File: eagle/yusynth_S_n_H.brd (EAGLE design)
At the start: 100 x 80 mm, 43 parts, among them IC1 TL074P, IC2 TL071P, Q1 BF245, T1 2N3904

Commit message: routed
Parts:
- moved R11 10.7 mm to (66.8, 34.3)
- moved C7 3.94 mm to (69.8, 33.3)
- moved LED1 2.05 mm to (44.2, 53.8)
- moved U$1 1.78 mm to (25.4, 55.4)
- moved R5 1.61 mm to (62.0, 46.2)
- moved R8 1.37 mm to (65.4, 40.1)
- moved R7 1.14 mm to (68.3, 42.7)
- moved C9 0.76 mm to (55.1, 41.9)
- moved R2 0.76 mm to (54.6, 53.8)
- moved R3 0.51 mm to (66.5, 25.4)
- turned C1 to 180 degrees
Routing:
- net -12V: track 62.9 -> 106.1 mm, vias 0 -> 2
- net GND: track 379.4 -> 369.5 mm
- net N$3: track 55.1 -> 46.4 mm
- net N$10: track 36.5 -> 29.1 mm
- net N$21: track 34.4 -> 27.2 mm, vias 2 -> 0
- net N$7: track 13.9 -> 11.8 mm
- net N$13: track 58.5 -> 56.5 mm
- net N$8: track 6.07 -> 4.17 mm
- net N$1: track 13.3 -> 11.9 mm
- net N$4: track 62.1 -> 63.3 mm
- net N$5: track 6.02 -> 5.08 mm
- net N$19: track 68.9 -> 68.2 mm
- net N$15: track 11.8 -> 11.2 mm

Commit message: cutout
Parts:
- moved SLEW 1.27 mm to (82.5, 3.81)
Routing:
- net GND: track 369.5 -> 373.4 mm
- net N$19: track 68.2 -> 69.5 mm
- net N$13: track 56.5 -> 57.7 mm
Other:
- board size 100 x 80 mm -> 100 x 81 mm
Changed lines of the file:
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@@
 <layer number="44" name="Drills" color="7" fill="1" visible="no" active="yes"/>
 <layer number="45" name="Holes" color="7" fill="1" visible="no" active="yes"/>
-<layer number="46" name="Milling" color="3" fill="1" visible="no" active="yes"/>
+<layer number="46" name="Milling" color="3" fill="1" visible="yes" active="yes"/>
 <layer number="47" name="Measures" color="7" fill="1" visible="no" active="yes"/>
 <layer number="48" name="Document" color="7" fill="1" visible="yes" active="yes"/>
@@
 <wire x1="100" y1="80" x2="0" y2="80" width="0" layer="20"/>
 <wire x1="0" y1="80" x2="0" y2="0" width="0" layer="20"/>
+<wire x1="2.286" y1="-1.016" x2="1.016" y2="0.762" width="1.6764" layer="46"/>
+<wire x1="1.016" y1="0.762" x2="1.016" y2="60.96" width="1.6764" layer="46"/>
+<wire x1="1.016" y1="60.96" x2="2.54" y2="62.23" width="1.6764" layer="46"/>
+<wire x1="2.54" y1="62.23" x2="90.424" y2="62.23" width="1.6764" layer="46"/>
+<wire x1="90.424" y1="62.23" x2="91.694" y2="60.452" width="1.6764" layer="46"/>
+<wire x1="91.694" y1="60.452" x2="91.694" y2="1.524" width="1.6764" layer="46"/>
+<wire x1="91.694" y1="1.524" x2="89.408" y2="-1.016" width="1.6764" layer="46"/>
+<wire x1="89.408" y1="-1.016" x2="2.286" y2="-1.016" width="1.6764" layer="46"/>
+<wire x1="5.08" y1="58.42" x2="4.572" y2="58.42" width="1.6764" layer="46"/>
+<wire x1="4.572" y1="58.42" x2="4.318" y2="58.166" width="1.6764" layer="46"/>
+<wire x1="4.318" y1="58.166" x2="4.318" y2="57.404" width="1.6764" layer="46"/>
+<wire x1="4.318" y1="57.404" x2="4.572" y2="57.15" width="1.6764" layer="46"/>
+<wire x1="4.572" y1="57.15" x2="5.08" y2="57.15" width="1.6764" layer="46"/>
+<wire x1="5.08" y1="57.15" x2="5.588" y2="57.658" width="1.6764" layer="46"/>
+<wire x1="5.588" y1="57.658" x2="5.588" y2="58.42" width="1.6764" layer="46"/>
+<wire x1="87.376" y1="58.928" x2="86.868" y2="58.928" width="1.6764" layer="46"/>
+<wire x1="86.868" y1="58.928" x2="86.614" y2="58.674" width="1.6764" layer="46"/>
+<wire x1="86.614" y1="58.674" x2="86.614" y2="57.912" width="1.6764" layer="46"/>
+<wire x1="86.614" y1="57.912" x2="86.868" y2="57.658" width="1.6764" layer="46"/>
+<wire x1="86.868" y1="57.658" x2="87.376" y2="57.658" width="1.6764" layer="46"/>
+<wire x1="87.376" y1="57.658" x2="87.884" y2="58.166" width="1.6764" layer="46"/>
+<wire x1="87.884" y1="58.166" x2="87.884" y2="58.928" width="1.6764" layer="46"/>
+<wire x1="5.334" y1="4.064" x2="4.826" y2="4.064" width="1.6764" layer="46"/>
+<wire x1="4.826" y1="4.064" x2="4.572" y2="3.81" width="1.6764" layer="46"/>
+<wire x1="4.572" y1="3.81" x2="4.572" y2="3.048" width="1.6764" layer="46"/>
+<wire x1="4.572" y1="3.048" x2="4.826" y2="2.794" width="1.6764" layer="46"/>
+<wire x1="4.826" y1="2.794" x2="5.334" y2="2.794" width="1.6764" layer="46"/>
+<wire x1="5.334" y1="2.794" x2="5.842" y2="3.302" width="1.6764" layer="46"/>
+<wire x1="5.842" y1="3.302" x2="5.842" y2="4.064" width="1.6764" layer="46"/>
 </plain>
 <attributes>
@@
 <element name="R8" library="rcl" package="0207/10" value="100k" x="65.405" y="40.132"/>
 <element name="R9" library="rcl" package="0207/10" value="100k" x="51.435" y="20.955" rot="R90"/>
-<element name="SLEW" library="pot" package="3RP/1610N" value="1M log" x="82.55" y="5.08"/>
+<element name="SLEW" library="pot" package="3RP/1610N" value="1M log" x="82.55" y="3.81"/>
 <element name="T1" library="transistor" package="TO92" value="2N3904" x="55.88" y="49.53" rot="R270"/>
 <element name="U$1" library="adafruit" package="FB" value="FB" x="25.4" y="55.372"/>
@@
 <wire x1="72.5424" y1="40.64" x2="72.5424" y2="42.672" width="0.8128" layer="16"/>
 <wire x1="89.6112" y1="23.1648" x2="72.5424" y2="40.2336" width="0.8128" layer="16"/>
-<wire x1="89.6112" y1="4.2672" x2="89.6112" y2="23.1648" width="0.8128" layer="16"/>
-<wire x1="88.392" y1="3.048" x2="89.6112" y2="4.2672" width="0.8128" layer="16"/>
-<wire x1="81.6864" y1="3.048" x2="88.392" y2="3.048" width="0.8128" layer="16"/>
-<wire x1="79.8576" y1="4.8768" x2="81.6864" y2="3.048" width="0.8128" layer="16"/>
-<wire x1="79.8576" y1="6.096" x2="79.8576" y2="4.8768" width="0.8128" layer="16"/>
+<wire x1="89.6112" y1="2.7432" x2="89.6112" y2="23.1648" width="0.8128" layer="16"/>
+<wire x1="88.392" y1="1.016" x2="89.6112" y2="2.7432" width="0.8128" layer="16"/>
+<wire x1="81.6864" y1="1.016" x2="88.392" y2="1.016" width="0.8128" layer="16"/>
+<wire x1="79.8576" y1="2.8448" x2="81.6864" y2="1.016" width="0.8128" layer="16"/>
+<wire x1="79.8576" y1="6.096" x2="79.8576" y2="2.8448" width="0.8128" layer="16"/>
 <wire x1="75.5904" y1="10.3632" x2="79.8576" y2="6.096" width="0.8128" layer="16"/>
 <wire x1="72.5424" y1="42.672" x2="73.406" y2="42.672" width="0.8128" layer="16"/>
@@
 <wire x1="82.9056" y1="5.4864" x2="82.9056" y2="12.192" width="0.8128" layer="16"/>
 <wire x1="82.9056" y1="12.192" x2="82.55" y2="12.7" width="0.8128" layer="16"/>
-<wire x1="82.9056" y1="5.4864" x2="82.55" y2="5.08" width="0.8128" layer="16"/>
+<wire x1="82.9056" y1="5.4864" x2="82.55" y2="3.81" width="0.8128" layer="16"/>
 <wire x1="58.5216" y1="25.6032" x2="58.5216" y2="28.6512" width="0.8128" layer="16"/>
 <wire x1="60.3504" y1="23.7744" x2="58.5216" y2="25.6032" width="0.8128" layer="16"/>
@@
 <wire x1="59.944" y1="32.9184" x2="64.6176" y2="32.9184" width="0.8128" layer="16"/>
 <wire x1="48.1584" y1="36.576" x2="50.165" y2="33.6804" width="0.8128" layer="16"/>
-<wire x1="87.4268" y1="5.4864" x2="87.55" y2="5.08" width="0.8128" layer="16"/>
+<wire x1="87.4268" y1="5.4864" x2="87.55" y2="3.81" width="0.8128" layer="16"/>
 <wire x1="48.1584" y1="36.576" x2="48.26" y2="36.83" width="0.8128" layer="16"/>
 </signal>

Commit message: gcode
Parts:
- moved C3 1.78 mm to (78.2, 12.7)
- moved C5 1.78 mm to (54.1, 24.1)
- moved IC1 1.78 mm to (54.1, 33.0)
- moved INT_EXT 1.78 mm to (38.6, 21.3)
- moved LIN_LOG 1.78 mm to (42.7, 42.8)
- moved OUT 1.78 mm to (69.3, 0.00)
- moved R11 1.78 mm to (65.0, 34.3)
- moved R3 1.78 mm to (64.8, 25.4)
- moved R9 1.78 mm to (49.7, 21.0)
- moved T1 1.78 mm to (54.1, 49.5)
- moved D1 1.78 mm to (31.2, 15.2)
- moved IC2 1.78 mm to (16.0, 29.2)
- moved RATE 1.78 mm to (26.2, 3.81)
- moved SIGNAL_IN 1.78 mm to (14.7, 0.00)
- moved C11 1.78 mm to (7.11, 22.9)
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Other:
- board size 100 x 81 mm -> 100.8 x 81 mm

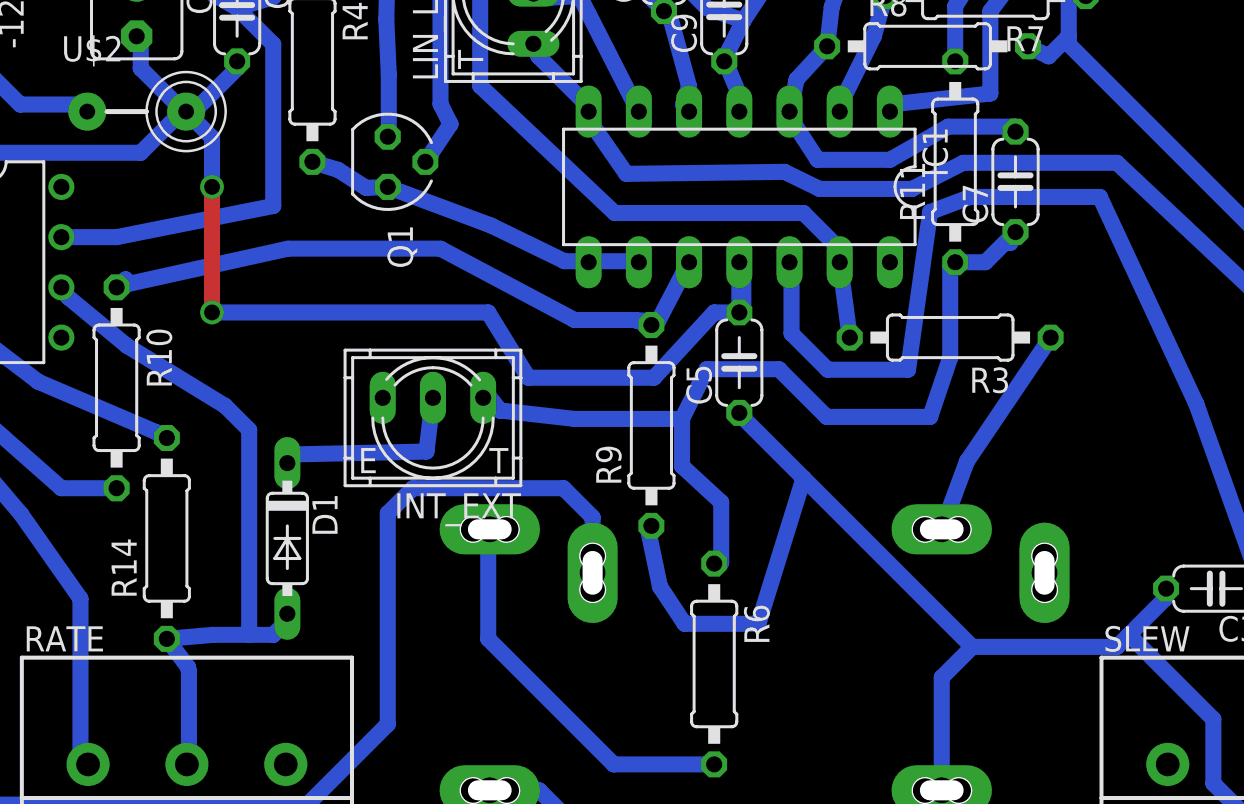
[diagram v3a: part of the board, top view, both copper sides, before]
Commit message: fixed an opamp output connection and spacing tweaks
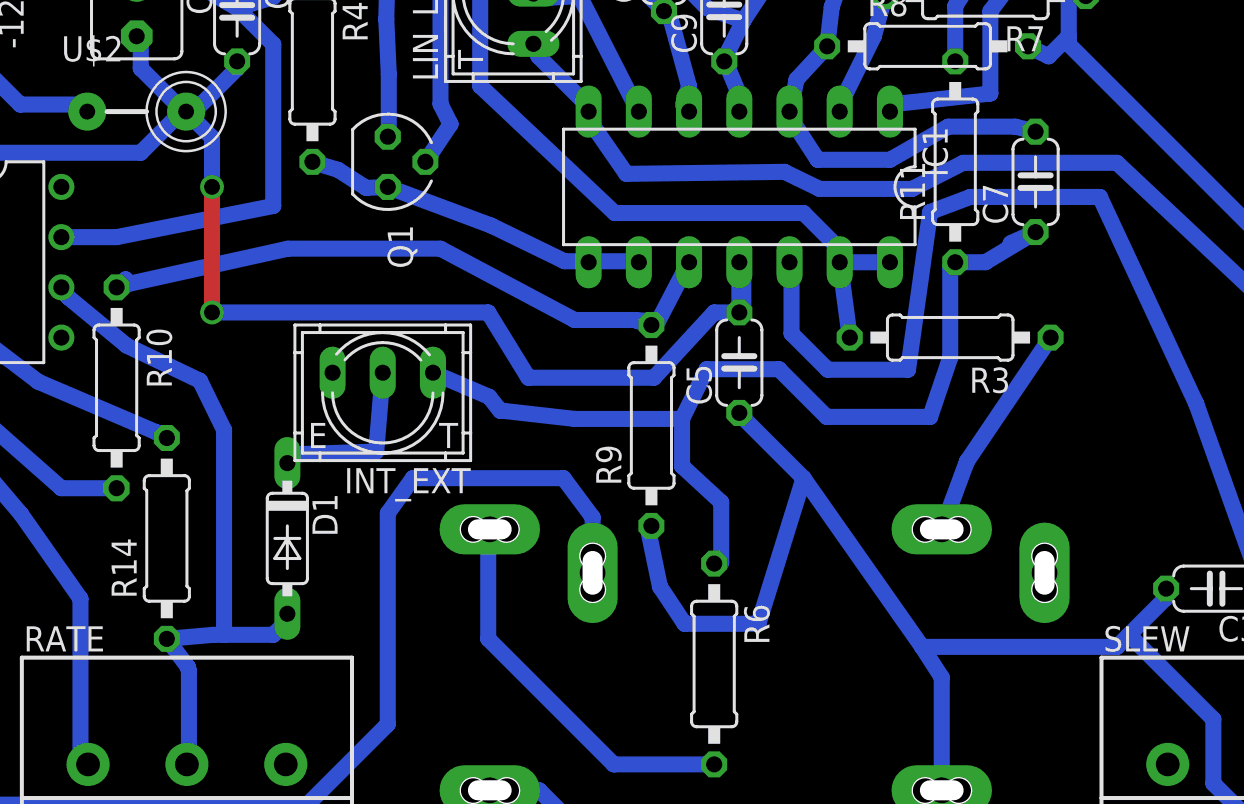
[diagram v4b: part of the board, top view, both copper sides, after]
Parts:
- moved INT_EXT 2.84 mm to (36.1, 22.6)
- moved C7 1.02 mm to (69.1, 33.3)
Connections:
- net N$11: now also IC1.14
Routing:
- net N$3: track 46.4 -> 50.8 mm
- net N$11: track 35.1 -> 37.6 mm
- net N$26: track 10.4 -> 9.08 mm
- net N$10: track 29.1 -> 29.8 mm
- net N$12: track 120.5 -> 121.3 mm
- net N$25: track 35.8 -> 35.1 mm
- net GND: track 373.4 -> 374.0 mm
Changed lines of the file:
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@@
 <element name="C5" library="rcl" package="C050-024X044" value="100n" x="54.102" y="24.13" rot="R90"/>
 <element name="C6" library="rcl" package="C050-024X044" value="100n" x="61.722" y="53.34" rot="R90"/>
-<element name="C7" library="rcl" package="C050-024X044" value="1n" x="68.072" y="33.274" rot="R90"/>
+<element name="C7" library="rcl" package="C050-024X044" value="1n" x="69.088" y="33.274" rot="R90"/>
 <element name="C8" library="rcl" package="C050-024X044" value="100n" x="28.702" y="41.91" rot="R270"/>
 <element name="C9" library="rcl" package="C050-024X044" value="100n" x="53.34" y="41.91" rot="R90"/>
@@
 <element name="U$1" library="adafruit" package="FB" value="FB" x="23.622" y="55.372"/>
 <element name="U$2" library="adafruit" package="FB" value="FB" x="23.622" y="36.83"/>
-<element name="INT_EXT" library="switch-misc" package="9077-1" value="9077-1" x="38.608" y="21.336" rot="R180"/>
+<element name="INT_EXT" library="switch-misc" package="9077-1" value="9077-1" x="36.068" y="22.606" rot="R180"/>
 <element name="IC2" library="linear" package="DIL08" value="TL071P" x="16.002" y="29.21" rot="R270"/>
 <element name="R12" library="rcl" package="0207/10" value="2k2" x="9.652" y="19.05"/>
@@
 <wire x1="70.4088" y1="42.7736" x2="72.0852" y2="45.8216" width="0.8128" layer="16"/>
 <wire x1="70.4088" y1="42.7736" x2="71.628" y2="42.672" width="0.8128" layer="16"/>
-<wire x1="65.8876" y1="9.7536" x2="57.3532" y2="18.288" width="0.8128" layer="16"/>
+<wire x1="63.3476" y1="9.7536" x2="57.3532" y2="18.288" width="0.8128" layer="16"/>
 <wire x1="57.3532" y1="18.288" x2="54.3052" y2="21.336" width="0.8128" layer="16"/>
-<wire x1="73.2028" y1="9.7536" x2="65.8876" y2="9.7536" width="0.8128" layer="16"/>
+<wire x1="73.2028" y1="9.7536" x2="63.3476" y2="9.7536" width="0.8128" layer="16"/>
 <wire x1="75.6412" y1="12.192" x2="73.8124" y2="10.3632" width="0.8128" layer="16"/>
 <wire x1="73.8124" y1="10.3632" x2="73.2028" y2="9.7536" width="0.8128" layer="16"/>
@@
 <wire x1="41.612896875" y1="51.054" x2="38.493640625" y2="51.12525625" width="0.8128" layer="16"/>
 <wire x1="64.342" y1="2.5" x2="64.342" y2="8.208" width="0.8128" layer="16"/>
-<wire x1="64.342" y1="8.208" x2="65.8876" y2="9.7536" width="0.8128" layer="16"/>
+<wire x1="64.342" y1="8.208" x2="63.3476" y2="9.7536" width="0.8128" layer="16"/>
 <wire x1="61.722" y1="55.88" x2="60.452" y2="56.2864" width="0.8128" layer="16"/>
 <wire x1="60.452" y1="56.2864" x2="59.3344" y2="56.388" width="0.8128" layer="16"/>
@@
 <wire x1="13.462" y1="59.7408" x2="13.462" y2="59.69" width="0.8128" layer="16"/>
 <wire x1="46.682" y1="13.5" x2="46.682" y2="16.31" width="0.8128" layer="16"/>
-<wire x1="46.682" y1="16.31" x2="45.212" y2="17.78" width="0.8128" layer="16"/>
-<wire x1="45.212" y1="17.78" x2="37.592" y2="17.78" width="0.8128" layer="16"/>
-<wire x1="37.592" y1="17.78" x2="36.322" y2="16.51" width="0.8128" layer="16"/>
+<wire x1="46.682" y1="16.31" x2="45.212" y2="18.288" width="0.8128" layer="16"/>
+<wire x1="45.212" y1="18.288" x2="37.592" y2="18.288" width="0.8128" layer="16"/>
+<wire x1="37.592" y1="18.288" x2="36.322" y2="16.51" width="0.8128" layer="16"/>
 <wire x1="36.322" y1="16.51" x2="36.322" y2="5.842" width="0.8128" layer="16"/>
 <wire x1="36.322" y1="5.842" x2="32.258" y2="1.778" width="0.8128" layer="16"/>
@@
 <wire x1="45.7708" y1="21.2852" x2="42.1894" y2="21.6916" width="0.8128" layer="16"/>
 <wire x1="51.2064" y1="21.2852" x2="45.7708" y2="21.2852" width="0.8128" layer="16"/>
-<wire x1="41.4528" y1="22.4028" x2="41.148" y2="22.352" width="0.8128" layer="16"/>
+<wire x1="41.4528" y1="22.4028" x2="38.608" y2="23.622" width="0.8128" layer="16"/>
 <wire x1="58.5216" y1="21.3868" x2="63.754" y2="21.3868" width="0.8128" layer="16"/>
 <wire x1="63.754" y1="21.3868" x2="64.77" y2="24.384" width="0.8128" layer="16"/>
-<wire x1="67.818" y1="30.1752" x2="68.072" y2="30.734" width="0.8128" layer="16"/>
+<wire x1="67.818" y1="30.1752" x2="69.088" y2="30.734" width="0.8128" layer="16"/>
 <wire x1="64.77" y1="24.384" x2="64.77" y2="28.956" width="0.8128" layer="16"/>
 <wire x1="64.77" y1="28.956" x2="65.024" y2="29.21" width="0.8128" layer="16"/>
 <wire x1="65.024" y1="29.21" x2="66.548" y2="29.21" width="0.8128" layer="16"/>
-<wire x1="66.548" y1="29.21" x2="68.072" y2="30.734" width="0.8128" layer="16"/>
+<wire x1="66.548" y1="29.21" x2="69.088" y2="30.734" width="0.8128" layer="16"/>
 </signal>
 <signal name="N$10">
@@
 <wire x1="58.0644" y1="34.3916" x2="61.722" y2="34.3916" width="0.8128" layer="16"/>
 <wire x1="56.642" y1="36.576" x2="58.0644" y2="34.3916" width="0.8128" layer="16"/>
-<wire x1="68.072" y1="36.068" x2="68.072" y2="35.814" width="0.8128" layer="16"/>
+<wire x1="68.072" y1="36.068" x2="69.088" y2="35.814" width="0.8128" layer="16"/>
 <wire x1="56.642" y1="36.576" x2="56.642" y2="36.83" width="0.8128" layer="16"/>
 <wire x1="62.3316" y1="47.6504" x2="64.7192" y2="48.9204" width="0.8128" layer="16"/>
@@
 <wire x1="59.182" y1="29.21" x2="59.182" y2="29.8704" width="0.8128" layer="16"/>
 <wire x1="42.6974" y1="45.2882" x2="43.688" y2="45.339" width="0.8128" layer="16"/>
+<contactref element="IC1" pad="14"/>
+<wire x1="59.182" y1="29.21" x2="61.722" y2="29.21" width="0.8128" layer="16"/>
 </signal>
 <signal name="N$13">
@@
 <contactref element="RATE" pad="2"/>
 <contactref element="R14" pad="1"/>
-<wire x1="30.5308" y1="10.3632" x2="29.3116" y2="10.3632" width="0.8128" layer="16"/>
-<wire x1="29.3116" y1="10.3632" x2="27.4828" y2="10.3632" width="0.8128" layer="16"/>
+<wire x1="30.5308" y1="10.3632" x2="28.0416" y2="10.3632" width="0.8128" layer="16"/>
+<wire x1="28.0416" y1="10.3632" x2="27.4828" y2="10.3632" width="0.8128" layer="16"/>
 <wire x1="31.1404" y1="10.9728" x2="30.5308" y2="10.3632" width="0.8128" layer="16"/>
 <wire x1="27.4828" y1="10.3632" x2="25.146" y2="10.16" width="0.8128" layer="16"/>
 <wire x1="31.1404" y1="10.9728" x2="31.242" y2="11.43" width="0.8128" layer="16"/>
 <wire x1="23.114" y1="24.9936" x2="20.1676" y2="27.432" width="0.8128" layer="16"/>
-<wire x1="28.0924" y1="21.9456" x2="23.114" y2="24.9936" width="0.8128" layer="16"/>
-<wire x1="29.3116" y1="20.7264" x2="28.0924" y2="21.9456" width="0.8128" layer="16"/>
-<wire x1="29.3116" y1="10.3632" x2="29.3116" y2="20.7264" width="0.8128" layer="16"/>
+<wire x1="26.8224" y1="23.2156" x2="23.114" y2="24.9936" width="0.8128" layer="16"/>
+<wire x1="28.0416" y1="20.7264" x2="26.8224" y2="23.2156" width="0.8128" layer="16"/>
+<wire x1="28.0416" y1="10.3632" x2="28.0416" y2="20.7264" width="0.8128" layer="16"/>
 <wire x1="20.1676" y1="27.432" x2="19.812" y2="27.94" width="0.8128" layer="16"/>
 <wire x1="26.2636" y1="8.5344" x2="26.2636" y2="4.2672" width="0.8128" layer="16"/>
@@
 <contactref element="D1" pad="C"/>
 <contactref element="INT_EXT" pad="2"/>
-<wire x1="31.1658" y1="19.4818" x2="38.2778" y2="19.6342" width="0.8128" layer="16"/>
+<wire x1="31.1658" y1="19.4818" x2="35.7378" y2="19.6342" width="0.8128" layer="16"/>
 <wire x1="31.1404" y1="19.5072" x2="31.1658" y2="19.4818" width="0.8128" layer="16"/>
-<wire x1="38.2778" y1="19.6342" x2="38.608" y2="22.352" width="0.8128" layer="16"/>
+<wire x1="35.7378" y1="19.6342" x2="36.068" y2="23.622" width="0.8128" layer="16"/>
 <wire x1="31.1404" y1="19.5072" x2="31.242" y2="19.05" width="0.8128" layer="16"/>
 </signal>
